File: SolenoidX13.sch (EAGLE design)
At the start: 24 parts, among them J1 SAMTEC-CLT-111-01-X-DJ, U1 ULN2003V12

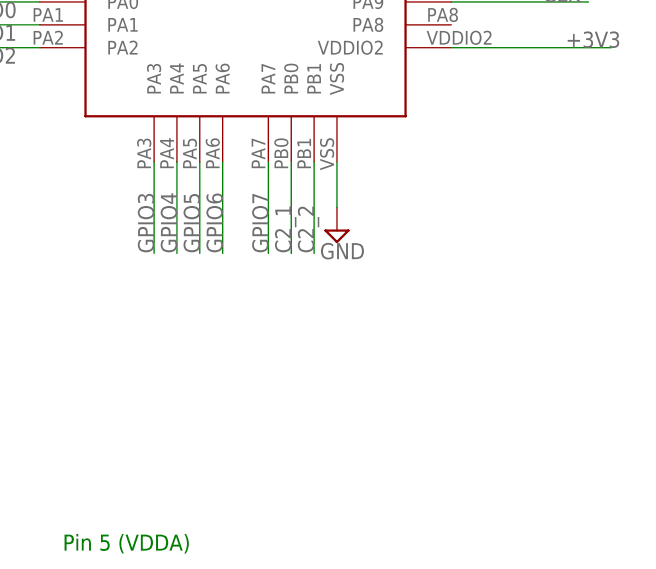
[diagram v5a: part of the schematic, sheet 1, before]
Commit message: it is smol now, cap gulag is gone, reset switch updated, clt part added to parts lib
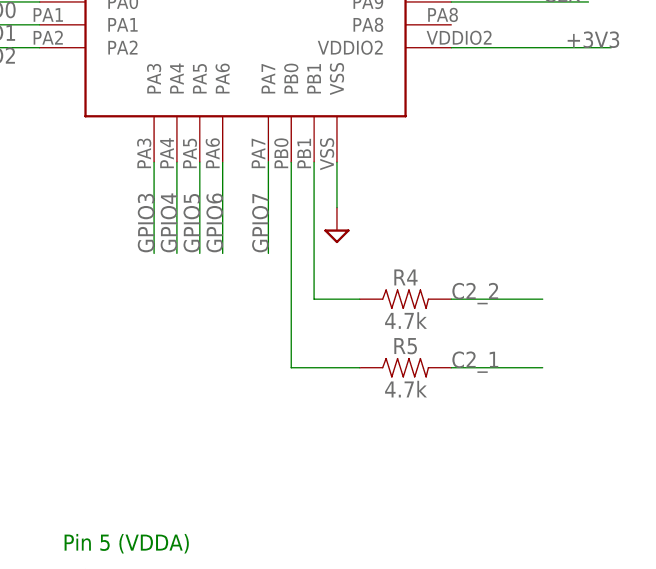
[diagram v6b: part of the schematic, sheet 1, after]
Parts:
- added R4, R5: 4.7k, SparkFun-Resistors:4.7KOHM-0603-1/10W-1%
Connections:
- new net N$1: R4.1, U$3.PB1
- new net N$2: R5.1, U$3.PB0
- net C2_1: now also R5.2; no longer U$3.PB0
- net C2_2: now also R4.2; no longer U$3.PB1
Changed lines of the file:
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@@
 <part name="SV1" library="con-lsta" library_urn="urn:adsk.eagle:library:161" deviceset="FE05-1" device="" package3d_urn="urn:adsk.eagle:package:8190/1"/>
 <part name="U$1" library="Push button - FSM2JMTR" deviceset="DISCRETECOMPONENTS_SWITCH" device="" package3d_urn="urn:adsk.eagle:package:24384574/2"/>
+<part name="R4" library="SparkFun-Resistors" library_urn="urn:adsk.eagle:library:532" deviceset="4.7KOHM" device="-0603-1/10W-1%" package3d_urn="urn:adsk.eagle:package:39650/1" value="4.7k"/>
+<part name="R5" library="SparkFun-Resistors" library_urn="urn:adsk.eagle:library:532" deviceset="4.7KOHM" device="-0603-1/10W-1%" package3d_urn="urn:adsk.eagle:package:39650/1" value="4.7k"/>
 </parts>
 <sheets>
@@
 <attribute name="VALUE" x="84.455" y="126.365" size="1.778" layer="96"/>
 </instance>
-<instance part="GND2" gate="GND" x="119.38" y="76.2" smashed="yes">
-<attribute name="VALUE" x="117.475" y="73.025" size="1.778" layer="96"/>
-</instance>
+<instance part="GND2" gate="GND" x="119.38" y="76.2" smashed="yes"/>
 <instance part="C7" gate="G$1" x="33.02" y="99.06" smashed="yes">
 <attribute name="NAME" x="34.544" y="101.981" size="1.778" layer="95" font="vector"/>
@@
 </instance>
 <instance part="U$1" gate="G$1" x="45.72" y="101.6" smashed="yes" rot="R90"/>
+<instance part="R4" gate="G$1" x="127" y="68.58" smashed="yes">
+<attribute name="NAME" x="127" y="70.104" size="1.778" layer="95" font="vector" align="bottom-center"/>
+<attribute name="VALUE" x="127" y="67.056" size="1.778" layer="96" font="vector" align="top-center"/>
+</instance>
+<instance part="R5" gate="G$1" x="127" y="60.96" smashed="yes">
+<attribute name="NAME" x="127" y="62.484" size="1.778" layer="95" font="vector" align="bottom-center"/>
+<attribute name="VALUE" x="127" y="59.436" size="1.778" layer="96" font="vector" align="top-center"/>
+</instance>
 </instances>
 <busses>
@@
 </segment>
 </net>
-<net name="C2_1" class="0">
-<segment>
-<wire x1="114.3" y1="73.66" x2="114.3" y2="83.82" width="0.1524" layer="91"/>
-<label x="114.3" y="73.66" size="1.778" layer="95" rot="R90"/>
-<pinref part="U$3" gate="G$1" pin="PB0"/>
-</segment>
-</net>
-<net name="C2_2" class="0">
-<segment>
-<wire x1="116.84" y1="73.66" x2="116.84" y2="83.82" width="0.1524" layer="91"/>
-<label x="116.84" y="73.66" size="1.778" layer="95" rot="R90"/>
-<pinref part="U$3" gate="G$1" pin="PB1"/>
-</segment>
-</net>
 <net name="GPIO0" class="0">
 <segment>
@@
 </segment>
 </net>
+<net name="C2_2" class="0">
+<segment>
+<wire x1="132.08" y1="68.58" x2="142.24" y2="68.58" width="0.1524" layer="91"/>
+<label x="132.08" y="68.58" size="1.778" layer="95"/>
+<pinref part="R4" gate="G$1" pin="2"/>
+</segment>
+</net>
+<net name="C2_1" class="0">
+<segment>
+<wire x1="132.08" y1="60.96" x2="142.24" y2="60.96" width="0.1524" layer="91"/>
+<label x="132.08" y="60.96" size="1.778" layer="95"/>
+<pinref part="R5" gate="G$1" pin="2"/>
+</segment>
+</net>
+<net name="N$1" class="0">
+<segment>
+<pinref part="U$3" gate="G$1" pin="PB1"/>
+<wire x1="116.84" y1="83.82" x2="116.84" y2="68.58" width="0.1524" layer="91"/>
+<pinref part="R4" gate="G$1" pin="1"/>
+<wire x1="116.84" y1="68.58" x2="121.92" y2="68.58" width="0.1524" layer="91"/>
+</segment>
+</net>
+<net name="N$2" class="0">
+<segment>
+<pinref part="U$3" gate="G$1" pin="PB0"/>
+<wire x1="114.3" y1="83.82" x2="114.3" y2="60.96" width="0.1524" layer="91"/>
+<pinref part="R5" gate="G$1" pin="1"/>
+<wire x1="114.3" y1="60.96" x2="121.92" y2="60.96" width="0.1524" layer="91"/>
+</segment>
+</net>

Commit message: ready for design review tbh
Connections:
- removed net NRST1: C7.1, R2.1, U$1.P$2, U$3.NRST
- net NRST: now also C7.1, R2.1, U$1.P$2, U$3.NRST
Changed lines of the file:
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@@
 </segment>
 </net>
-<net name="NRST1" class="0">
+<net name="NRST" class="0">
 <segment>
 <pinref part="C7" gate="G$1" pin="1"/>
@@
 <pinref part="U$1" gate="G$1" pin="P$2"/>
 <junction x="45.72" y="109.22"/>
+<label x="73.66" y="109.22" size="1.778" layer="95"/>
 </segment>
 </net>
